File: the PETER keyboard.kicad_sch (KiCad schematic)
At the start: 139 parts, among them J1 USB_C_Receptacle_USB2.0, SW1 RotaryEncoder_Switch, SW12 RotaryEncoder_Switch, SW2 SW_Push, U1 ATmega32U4-M, Y1 Crystal_GND24_Small

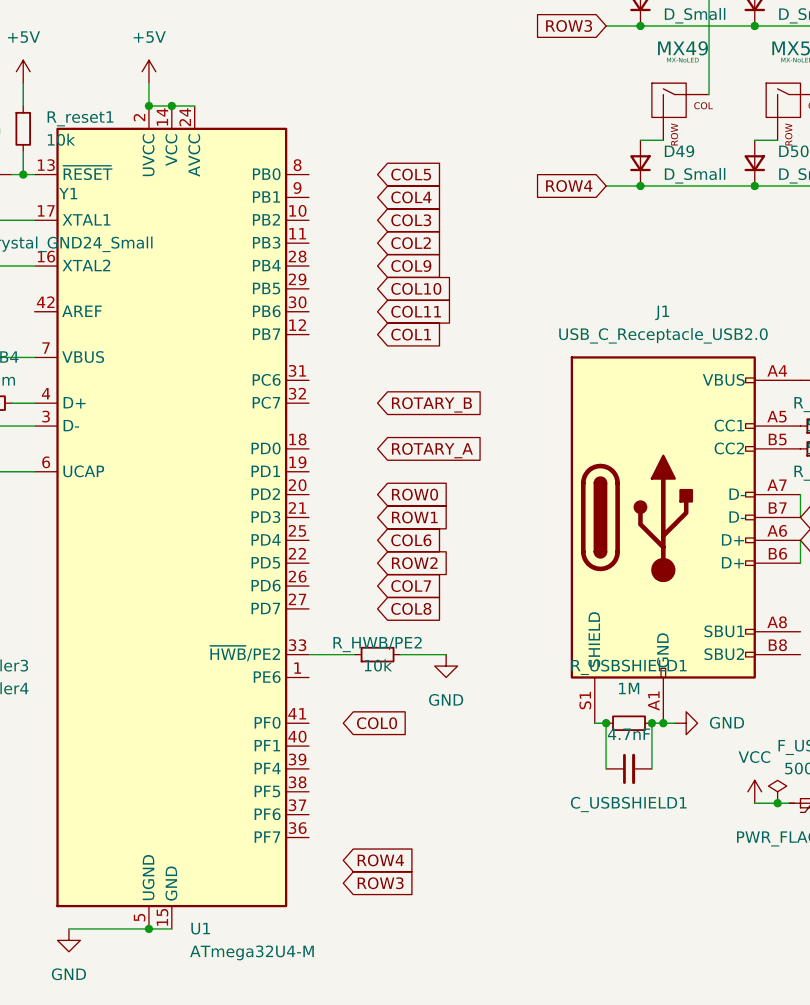
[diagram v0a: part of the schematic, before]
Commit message: traces added for rows and columns
rotary encoders are still left
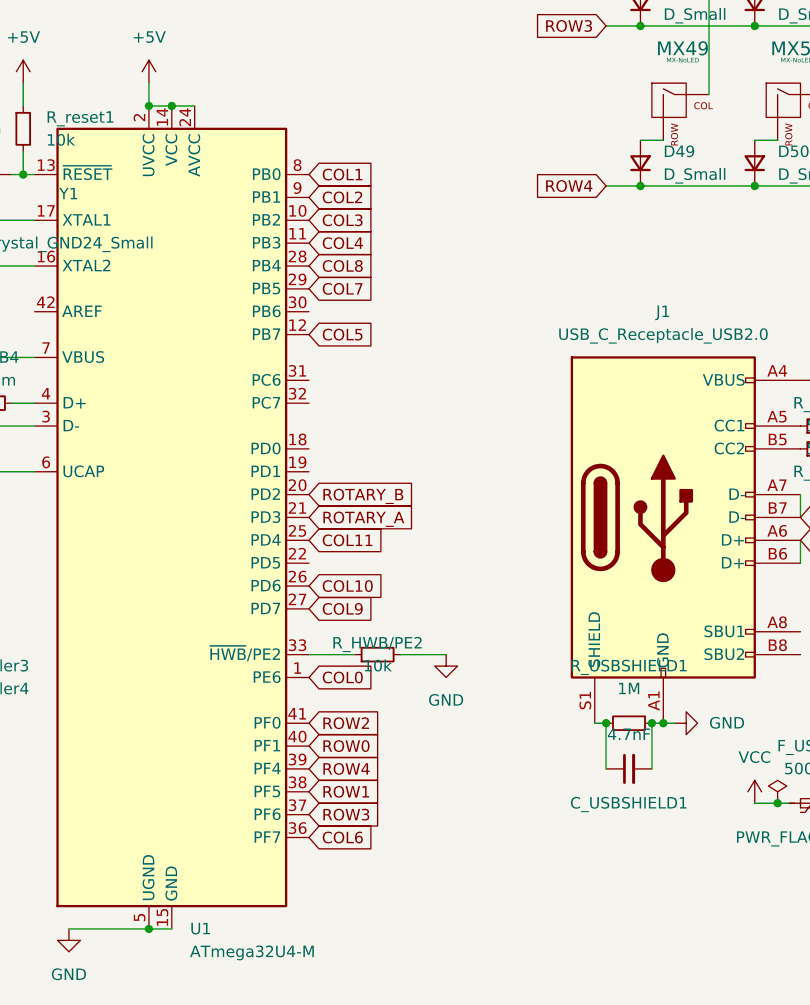
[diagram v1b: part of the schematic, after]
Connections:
- net  ROW3: now also U1.37 (PF6)
- net COL0: now also U1.1 (PE6)
- net COL1: now also U1.8 (PB0)
- net COL10: now also U1.26 (PD6)
- net COL11: now also U1.25 (PD4)
- net COL2: now also U1.9 (PB1)
- net COL3: now also U1.10 (PB2)
- net COL4: now also U1.11 (PB3)
- net COL5: now also U1.12 (PB7)
- net COL6: now also U1.36 (PF7)
- net COL7: now also U1.29 (PB5)
- net COL8: now also U1.28 (PB4)
- net COL9: now also U1.27 (PD7)
- net ROTARY_A: now also U1.21 (PD3)
- net ROTARY_B: now also U1.20 (PD2)
- net ROW0: now also U1.40 (PF1)
- net ROW1: now also U1.38 (PF5)
- net ROW2: now also U1.41 (PF0)
- net ROW4: now also U1.39 (PF4)

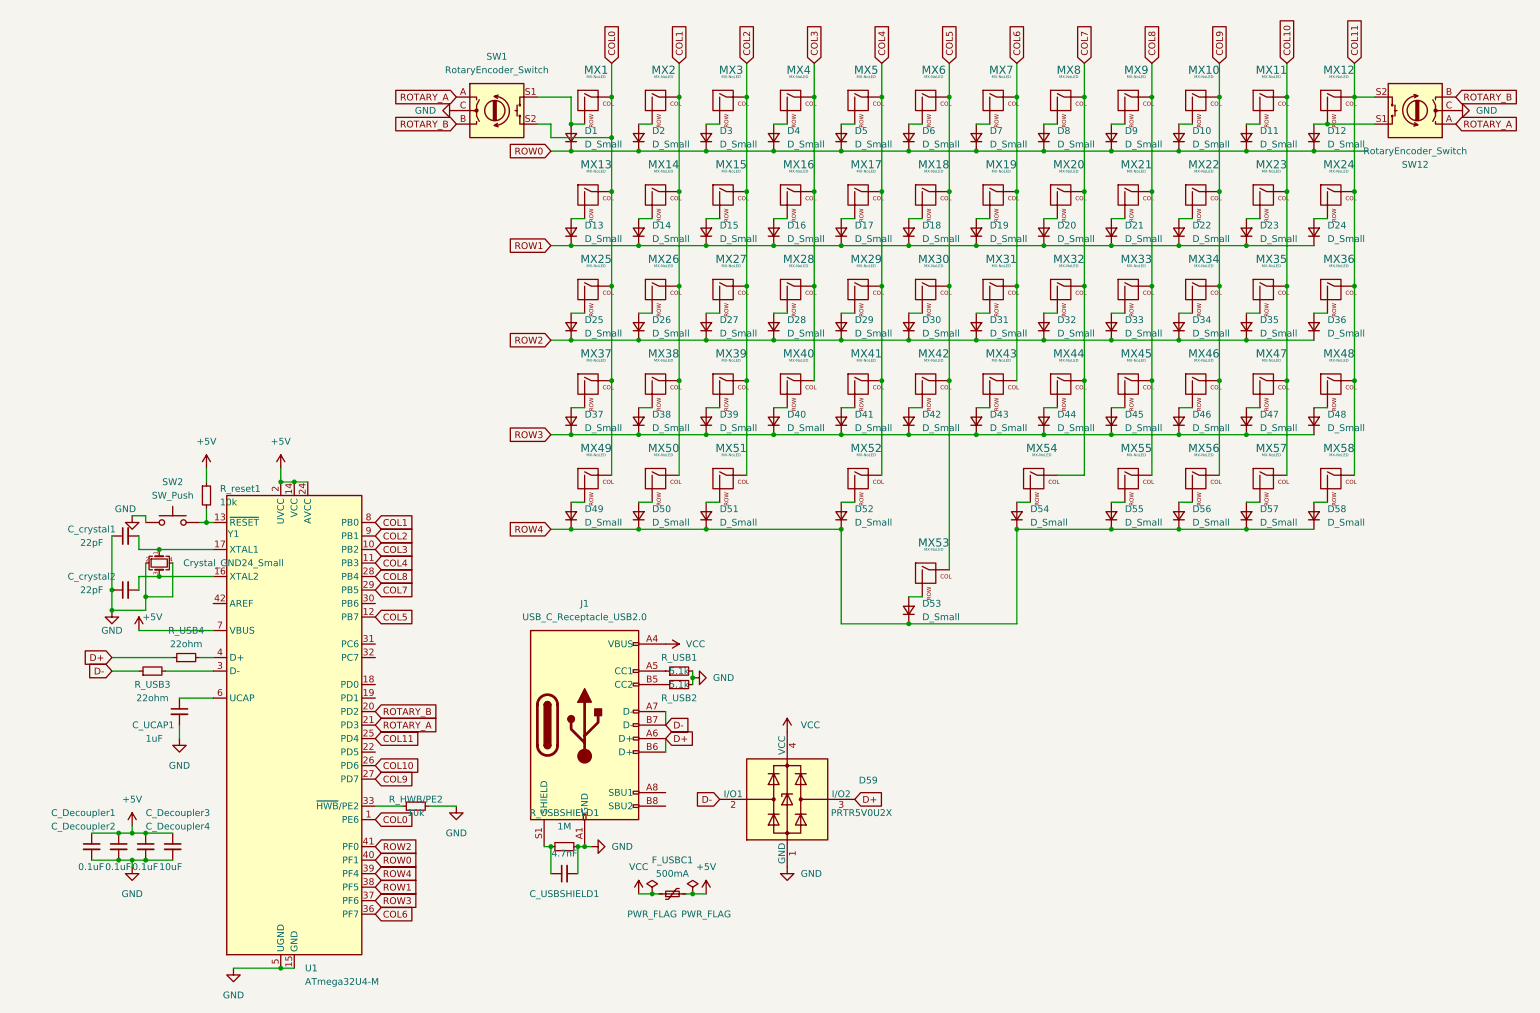
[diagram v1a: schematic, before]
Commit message: starting to redo mcu and usb
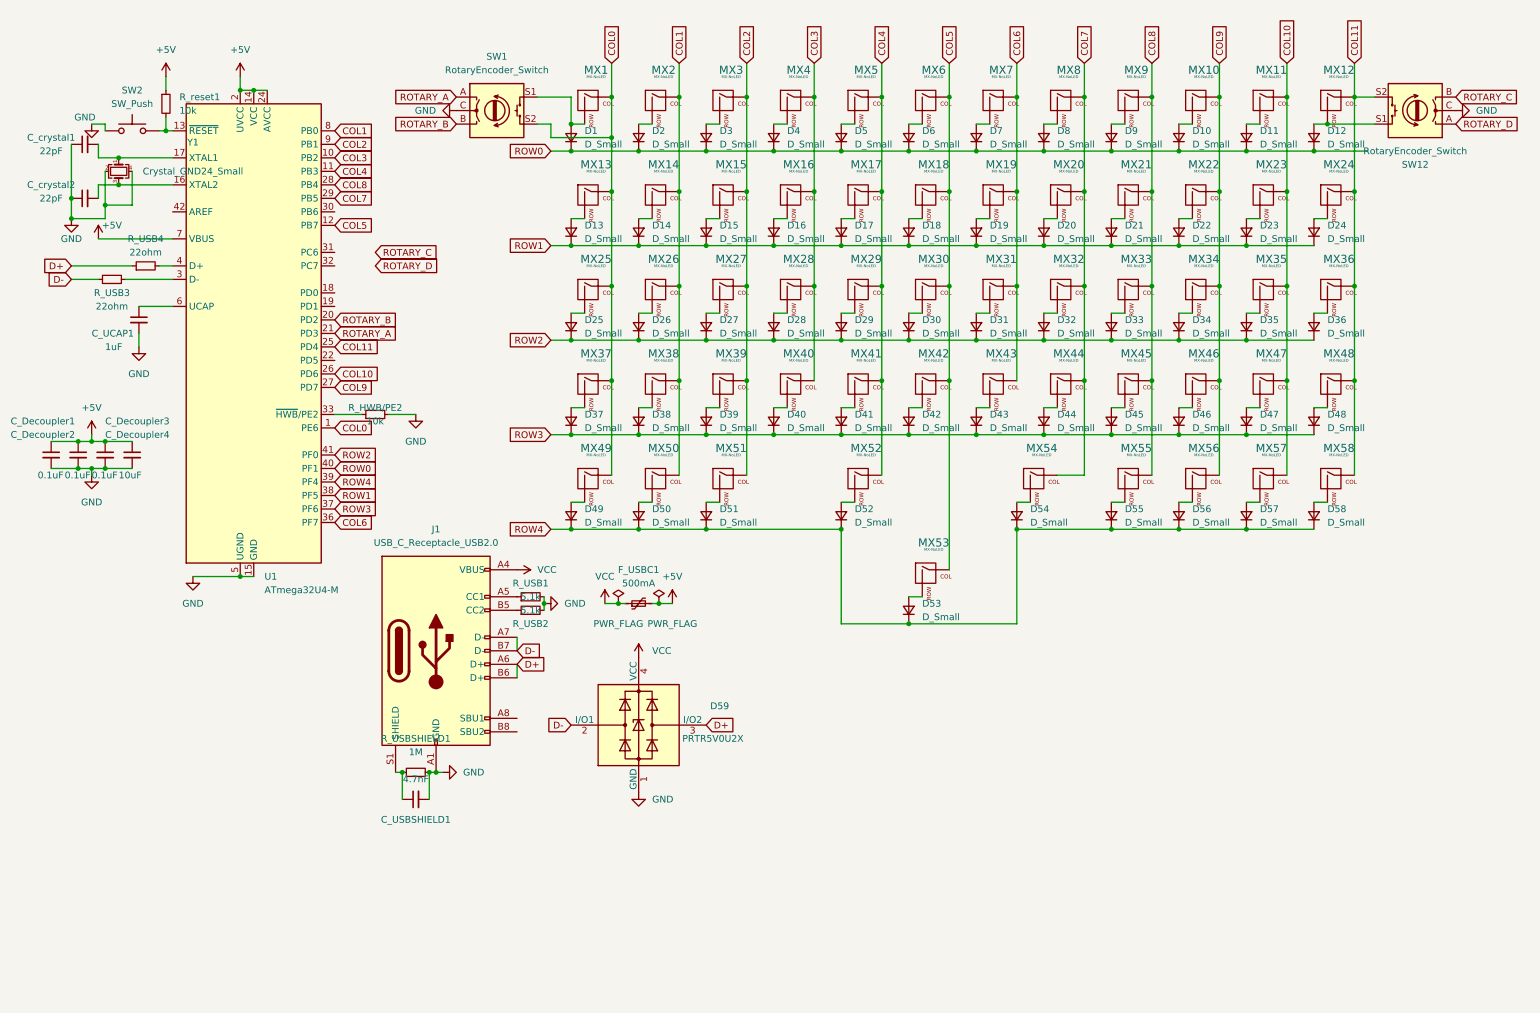
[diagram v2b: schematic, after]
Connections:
- net ROTARY_A: no longer SW12.A
- net ROTARY_B: no longer SW12.B
- new net ROTARY_C: SW12.B
- new net ROTARY_D: SW12.A
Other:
- moved on the sheet: C_Decoupler1, C_Decoupler2, C_Decoupler3, C_Decoupler4, C_UCAP1, C_USBSHIELD1, C_crystal1, C_crystal2, D59, F_USBC1, J1, R_HWB/PE2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

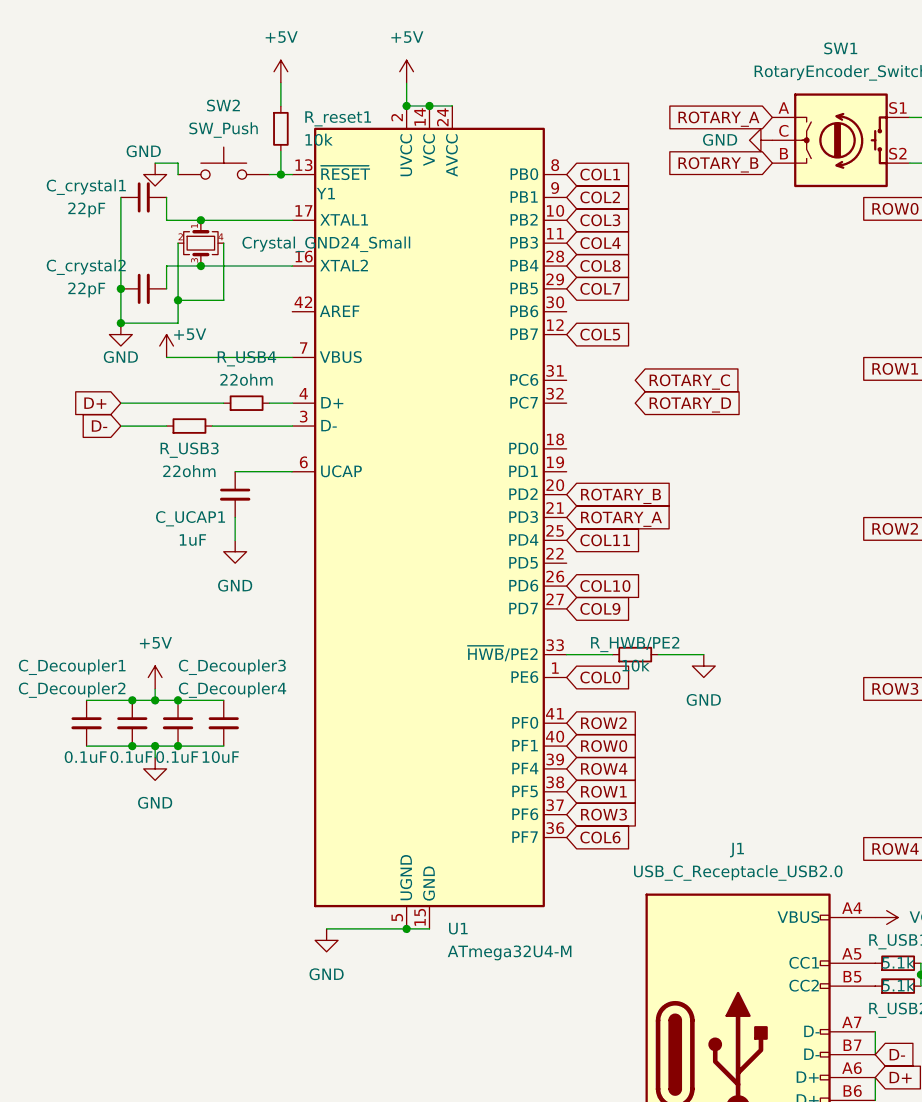
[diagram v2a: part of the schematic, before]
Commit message: cleaned up MCU, USB. Connected rows. Assigned to MCU. now routing rows & cols
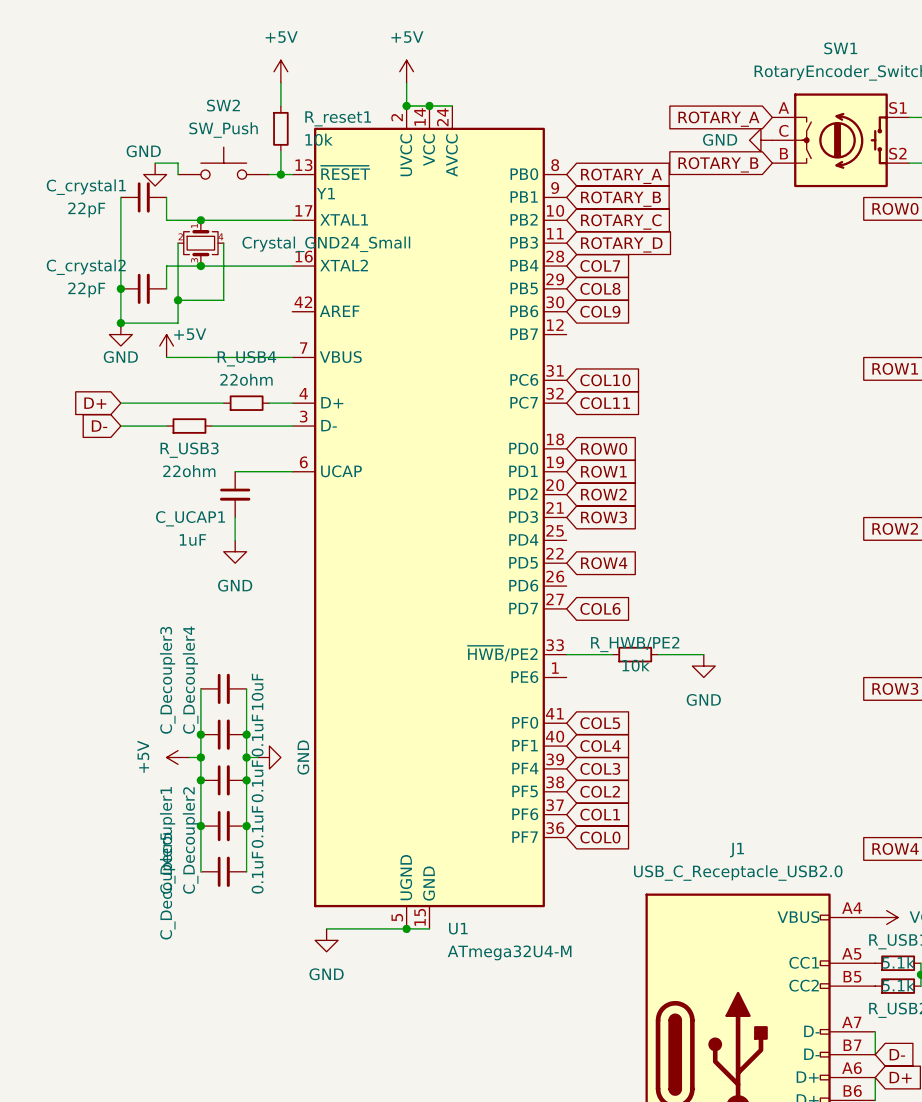
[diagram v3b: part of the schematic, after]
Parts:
- added C_Decoupler5: 0.1uF, Capacitor_SMD:C_0402_1005Metric, symbol Device:C_Small
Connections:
- net  ROW3: now also U1.21 (PD3); no longer U1.37 (PF6)
- net +5V: now also C_Decoupler5.1
- net COL0: now also U1.36 (PF7); no longer U1.1 (PE6)
- net COL1: now also U1.37 (PF6); no longer U1.8 (PB0)
- net COL10: now also U1.31 (PC6); no longer U1.26 (PD6)
- net COL11: now also U1.32 (PC7); no longer U1.25 (PD4)
- net COL2: now also U1.38 (PF5); no longer U1.9 (PB1)
- net COL3: now also U1.39 (PF4); no longer U1.10 (PB2)
- net COL4: now also U1.40 (PF1); no longer U1.11 (PB3)
- net COL5: now also U1.41 (PF0); no longer U1.12 (PB7)
- net COL6: now also U1.27 (PD7); no longer U1.36 (PF7)
- net COL7: now also U1.28 (PB4); no longer U1.29 (PB5)
- net COL8: now also U1.29 (PB5); no longer U1.28 (PB4)
- net COL9: now also U1.30 (PB6); no longer U1.27 (PD7)
- net GND: now also C_Decoupler5.2
- net ROTARY_A: now also U1.8 (PB0); no longer U1.21 (PD3)
- net ROTARY_B: now also U1.9 (PB1); no longer U1.20 (PD2)
- net ROTARY_C: now also U1.10 (PB2)
- net ROTARY_D: now also U1.11 (PB3)
- net ROW0: now also U1.18 (PD0); no longer U1.40 (PF1)
- net ROW1: now also U1.19 (PD1); no longer U1.38 (PF5)
- net ROW2: now also U1.20 (PD2); no longer U1.41 (PF0)
- net ROW4: now also U1.22 (PD5); no longer U1.39 (PF4)
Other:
- moved on the sheet: C_Decoupler1, C_Decoupler2, C_Decoupler3, C_Decoupler4

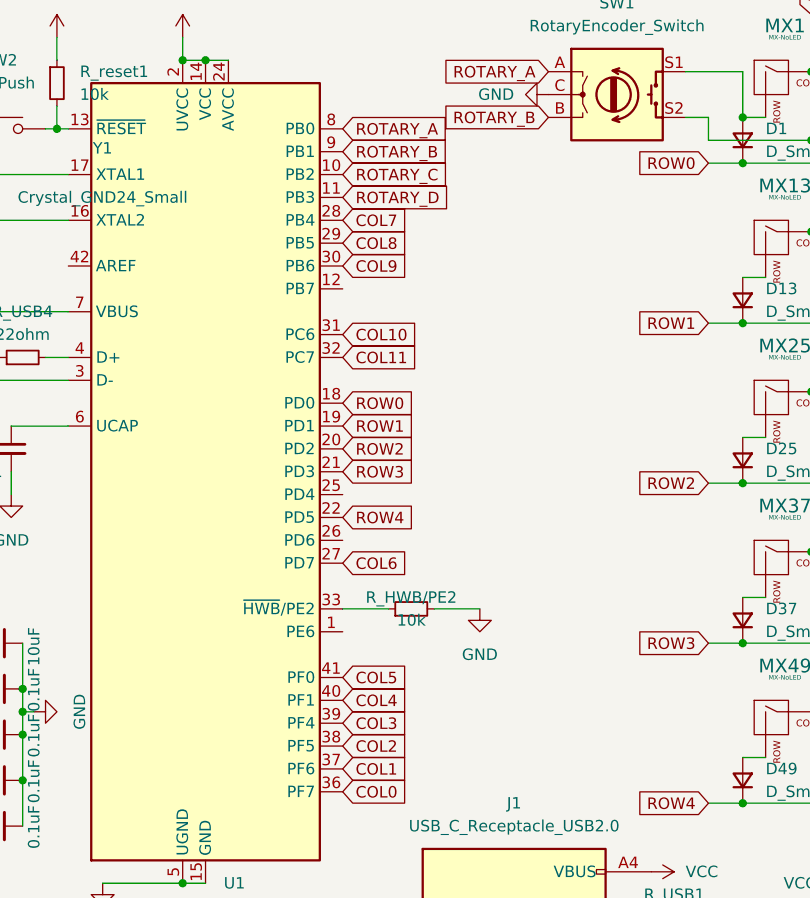
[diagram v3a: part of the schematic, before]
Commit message: all traces routed
no curves, no grounding routes drawn
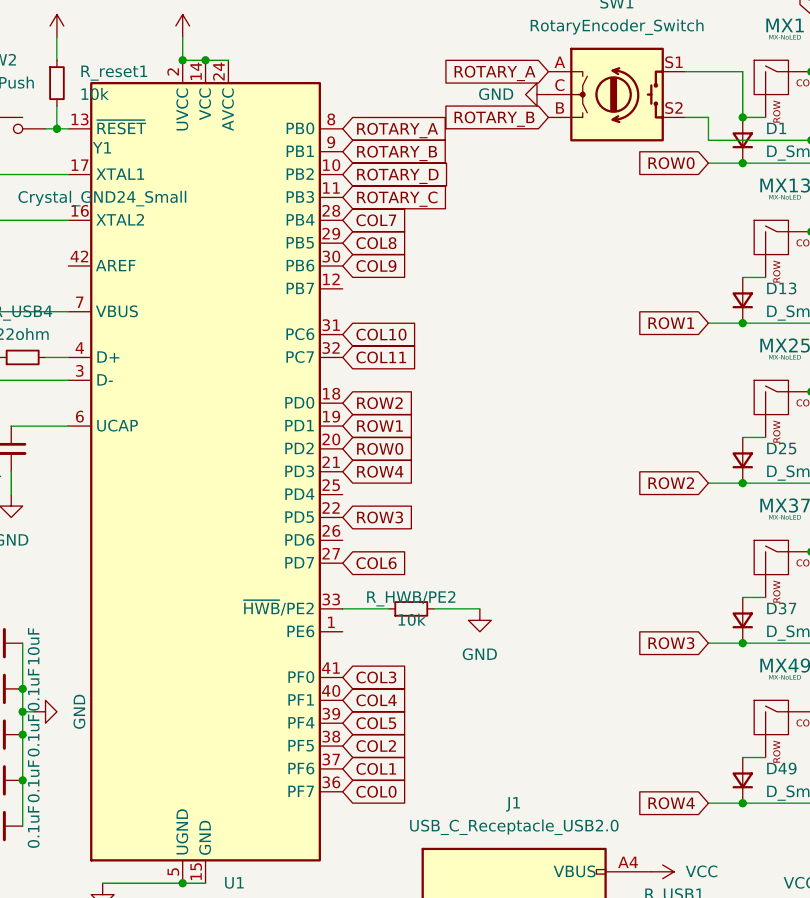
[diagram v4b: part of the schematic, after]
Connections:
- net  ROW3: now also U1.22 (PD5); no longer U1.21 (PD3)
- net COL3: now also U1.41 (PF0); no longer U1.39 (PF4)
- net COL5: now also U1.39 (PF4); no longer U1.41 (PF0)
- net ROTARY_C: now also U1.11 (PB3); no longer U1.10 (PB2)
- net ROTARY_D: now also U1.10 (PB2); no longer U1.11 (PB3)
- net ROW0: now also U1.20 (PD2); no longer U1.18 (PD0)
- net ROW2: now also U1.18 (PD0); no longer U1.20 (PD2)
- net ROW4: now also U1.21 (PD3); no longer U1.22 (PD5)

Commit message: added hotswap and mounting holes for reference
need to add cuts to pcb, reroute matrix and usb, mcu
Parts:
- MX1, MX10, MX11, MX12, MX13, MX14, MX15, MX16, MX17, MX18, MX19, MX2, MX20, MX21, MX22, MX23, MX26, MX27, MX28, MX29, MX3, MX30, MX31, MX32, MX33, MX34, MX35, MX38, MX39, MX4, MX40, MX41, MX42, MX43, MX44, MX45, MX46, MX47, MX48, MX5, MX50, MX55, MX56, MX57, MX58, MX6, MX7, MX8, MX9: footprint MX_Only:MXOnly-1U-NoLED -> MX_Only:MXOnly-1U-Hotswap
- MX24, MX37: footprint MX_Only:MXOnly-1.5U-NoLED -> MX_Only:MXOnly-1.5U-Hotswap
- MX25, MX36, MX49, MX51: footprint MX_Only:MXOnly-1.25U-NoLED -> MX_Only:MXOnly-1.25U-Hotswap
- MX52: footprint MX_Only:MXOnly-2.75U-NoLED -> MX_Only:MXOnly-2.75U-Hotswap
- MX53: footprint MX_Only:MXOnly-6U-Centered-NoLED -> MX_Only:MXOnly-6U-Centered-Hotswap
- MX54: footprint MX_Only:MXOnly-2.25U-NoLED -> MX_Only:MXOnly-2.25U-Hotswap

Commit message: rerouting
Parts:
- MX53: footprint MX_Only:MXOnly-6U-Centered-Hotswap -> MX_Only:MXOnly-6U-Centered-NoLED
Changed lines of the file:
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@@
       (effects (font (size 0.508 0.508)))
     )
-    (property "Footprint" "MX_Only:MXOnly-6U-Centered-Hotswap" (id 2) (at 156.845 116.205 0)
+    (property "Footprint" "MX_Only:MXOnly-6U-Centered-NoLED" (id 2) (at 156.845 116.205 0)
       (effects (font (size 1.524 1.524)) hide)
     )
@@
     )
     (path "/0870f4c6-cf74-4d41-94d2-7eecd22517a4"
-      (reference "MX53") (unit 1) (value "MX-NoLED") (footprint "MX_Only:MXOnly-6U-Centered-Hotswap")
+      (reference "MX53") (unit 1) (value "MX-NoLED") (footprint "MX_Only:MXOnly-6U-Centered-NoLED")
     )
     (path "/150cbac0-f7f3-42a2-9fee-ab866a5399d2"
